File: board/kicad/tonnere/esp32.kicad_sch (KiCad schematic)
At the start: 11 parts, among them J18 ESP PGM, J23 ESP JTAG, U34 ESP32-WROVER-E-N8R8

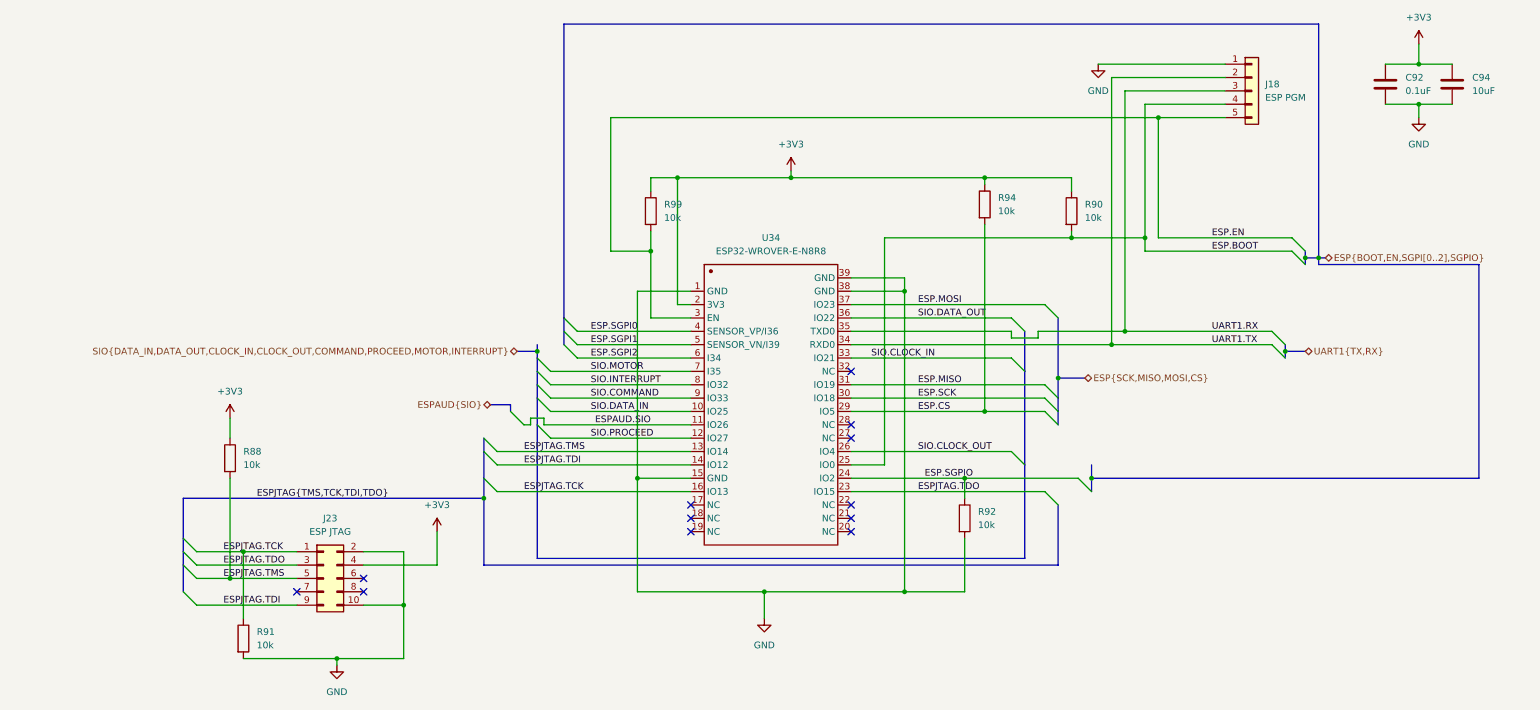
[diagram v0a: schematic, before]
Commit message: 0.60 (not final). Fix errata from 0.51. Added USB2 phy.
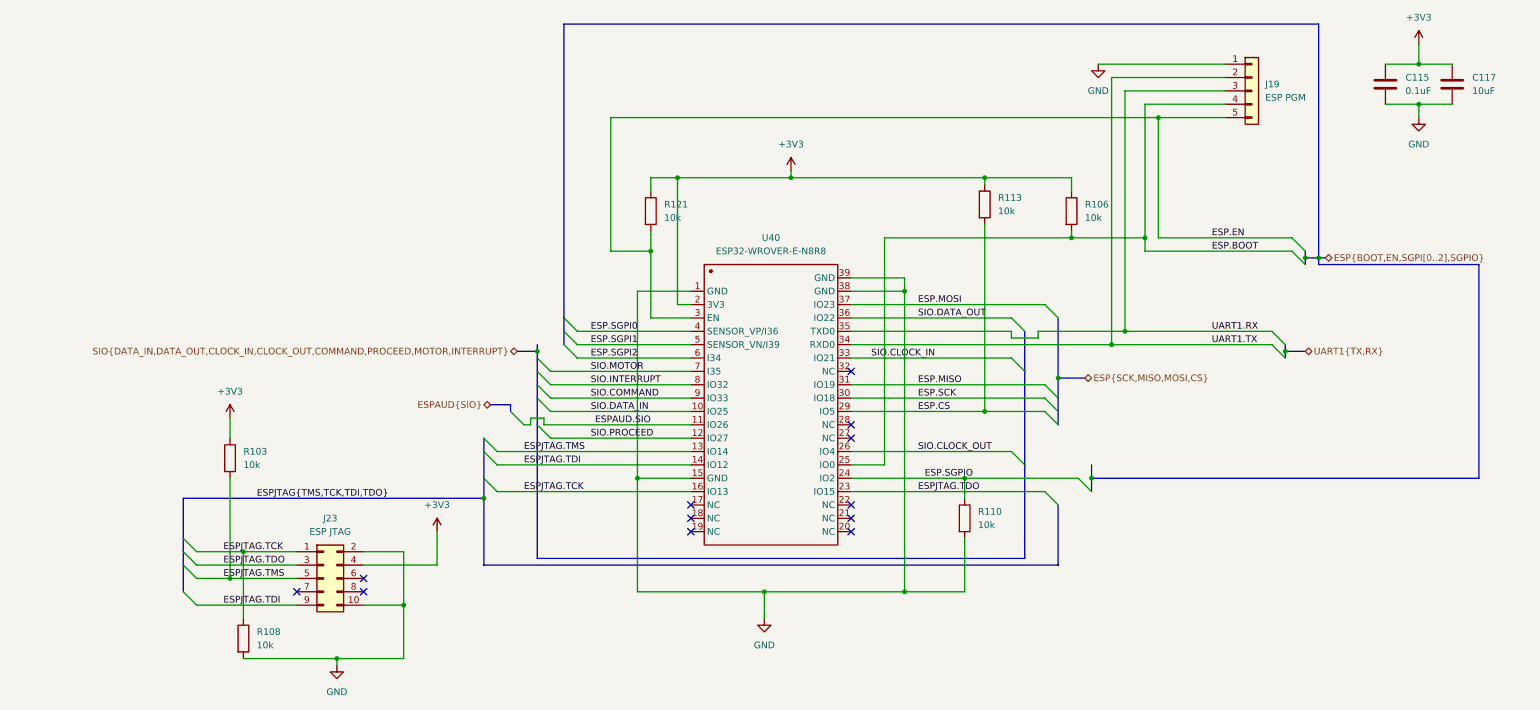
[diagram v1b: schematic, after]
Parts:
- renumbered C92 to C115, C94 to C117, J18 to J19, R88 to R103, R90 to R106, R91 to R108, R92 to R110, R94 to R113, R99 to R121, U34 to U40
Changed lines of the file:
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@@
 		(dnp no)
 		(fields_autoplaced yes)
-		(property "Reference" "R92"
+		(property "Reference" "R110"
 			(at 173.99 149.8599 0)
 			(effects
@@
 			(project "tonnere"
 				(path "/eb8e239c-f2ec-4b57-8f5c-6c75d6b59ab3/46474bdc-762b-418e-b7cb-754958627956"
-					(reference "R92")
+					(reference "R110")
 					(unit 1)
 				)
@@
 		(dnp no)
 		(fields_autoplaced yes)
-		(property "Reference" "R88"
+		(property "Reference" "R103"
 			(at 34.29 138.4299 0)
 			(effects
@@
 			(project "tonnere"
 				(path "/eb8e239c-f2ec-4b57-8f5c-6c75d6b59ab3/46474bdc-762b-418e-b7cb-754958627956"
-					(reference "R88")
+					(reference "R103")
 					(unit 1)
 				)
@@
 		(dnp no)
 		(fields_autoplaced yes)
-		(property "Reference" "R99"
+		(property "Reference" "R121"
 			(at 114.3 91.4399 0)
 			(effects
@@
 			(project ""
 				(path "/eb8e239c-f2ec-4b57-8f5c-6c75d6b59ab3/46474bdc-762b-418e-b7cb-754958627956"
-					(reference "R99")
+					(reference "R121")
 					(unit 1)
 				)
@@
 		(dnp no)
 		(fields_autoplaced yes)
-		(property "Reference" "R91"
+		(property "Reference" "R108"
 			(at 36.83 172.7199 0)
 			(effects
@@
 			(project "tonnere"
 				(path "/eb8e239c-f2ec-4b57-8f5c-6c75d6b59ab3/46474bdc-762b-418e-b7cb-754958627956"
-					(reference "R91")
+					(reference "R108")
 					(unit 1)
 				)
@@
 		(dnp no)
 		(fields_autoplaced yes)
-		(property "Reference" "R90"
+		(property "Reference" "R106"
 			(at 194.31 91.4399 0)
 			(effects
@@
 			(project "tonnere"
 				(path "/eb8e239c-f2ec-4b57-8f5c-6c75d6b59ab3/46474bdc-762b-418e-b7cb-754958627956"
-					(reference "R90")
+					(reference "R106")
 					(unit 1)
 				)
@@
 		(dnp no)
 		(fields_autoplaced yes)
-		(property "Reference" "C94"
+		(property "Reference" "C117"
 			(at 267.97 67.3099 0)
 			(effects
@@
 			(project "tonnere"
 				(path "/eb8e239c-f2ec-4b57-8f5c-6c75d6b59ab3/46474bdc-762b-418e-b7cb-754958627956"
-					(reference "C94")
+					(reference "C117")
 					(unit 1)
 				)
@@
 		(dnp no)
 		(fields_autoplaced yes)
-		(property "Reference" "J18"
+		(property "Reference" "J19"
 			(at 228.6 68.5799 0)
 			(effects
@@
 			(project ""
 				(path "/eb8e239c-f2ec-4b57-8f5c-6c75d6b59ab3/46474bdc-762b-418e-b7cb-754958627956"
-					(reference "J18")
+					(reference "J19")
 					(unit 1)
 				)
@@
 		(on_board yes)
 		(dnp no)
-		(property "Reference" "C92"
+		(property "Reference" "C115"
 			(at 255.27 67.3099 0)
 			(effects
@@
 			(project "tonnere"
 				(path "/eb8e239c-f2ec-4b57-8f5c-6c75d6b59ab3/46474bdc-762b-418e-b7cb-754958627956"
-					(reference "C92")
+					(reference "C115")
 					(unit 1)
 				)
@@
 		(dnp no)
 		(fields_autoplaced yes)
-		(property "Reference" "R94"
+		(property "Reference" "R113"
 			(at 177.8 90.1699 0)
 			(effects
@@
 			(project "tonnere"
 				(path "/eb8e239c-f2ec-4b57-8f5c-6c75d6b59ab3/46474bdc-762b-418e-b7cb-754958627956"
-					(reference "R94")
+					(reference "R113")
 					(unit 1)
 				)
@@
 		(dnp no)
 		(fields_autoplaced yes)
-		(property "Reference" "U34"
+		(property "Reference" "U40"
 			(at 134.62 97.79 0)
 			(effects
@@
 			(project ""
 				(path "/eb8e239c-f2ec-4b57-8f5c-6c75d6b59ab3/46474bdc-762b-418e-b7cb-754958627956"
-					(reference "U34")
-					(unit 1)
-				)
+					(reference "U40")
+					(unit 1)
+				)
